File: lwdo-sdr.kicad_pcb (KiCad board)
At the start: 2 copper layers, 162 x 120 mm, 360 parts, among them J101 IN1, J102 IN2, J103 IN3, J104 IN4, J105 USB_B, J106 CLK_OUT, J107 REF_IN, J1401 Conn_02x10_Odd_Even, Q1201 NX7002AK, Q1202 PMN48XP, U1001 74LVC1G157, U1002 74LVC2G04, U1101 74LVC2GU04, U1102 74LVC2G04, U1201 TL431AFDT, U1202 TL431AFDT, U1203 TL431AFDT, U1204 MCP1824T-330, U1205 NCV8164ASN120T1G, U1206 MCP1824T-330, U1207 NCV8164ASN250T1G, U1208 NCV8164ASN330T1G, U1301 AT93C56, U1302 FT2232HL, U1401 74AVC4T245PW, U1402 74AVC4T245PW, U201 ICE40HX4K, U202 W25Q16JV, U203 IS61WV25616FBLL-10TLI, U301 THS4521ID, U401 THS4521ID, U501 THS4521ID, U601 THS4521ID, U701 AD7357xRU, U801 AD7357xRU, U901 DAC8551, U902 MCP1501-33xSN, U903 NCS325, U904 74LVC2GU04, U905 74LVC2G04, X901 DOT050V-020.0M, Y1301 12MHz CL=18p

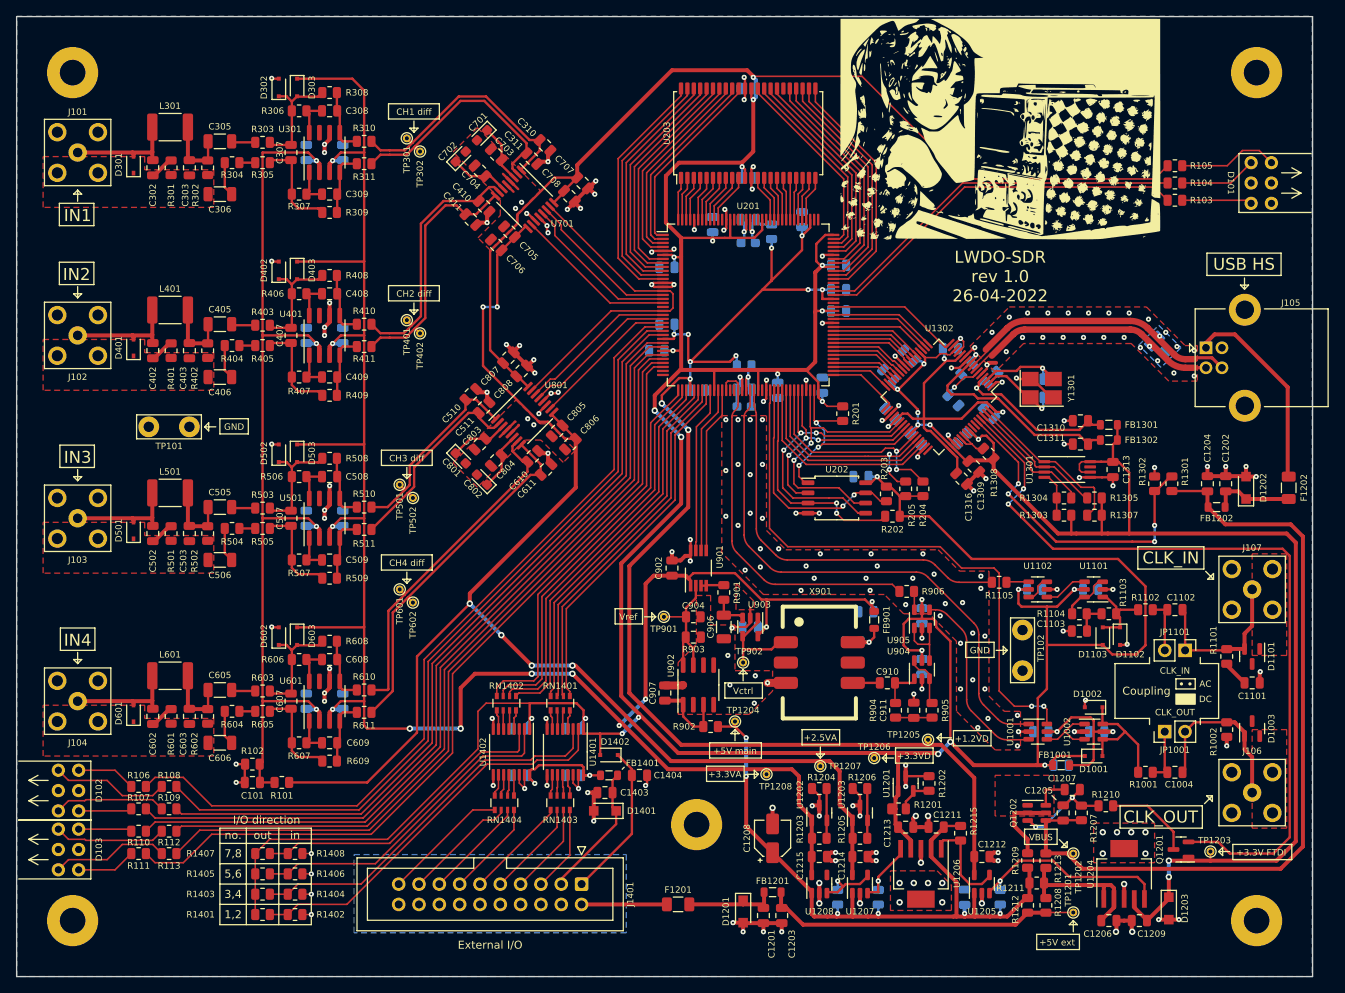
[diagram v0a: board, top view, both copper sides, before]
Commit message: Use standard Molex 73251-2201 footprint for SMA
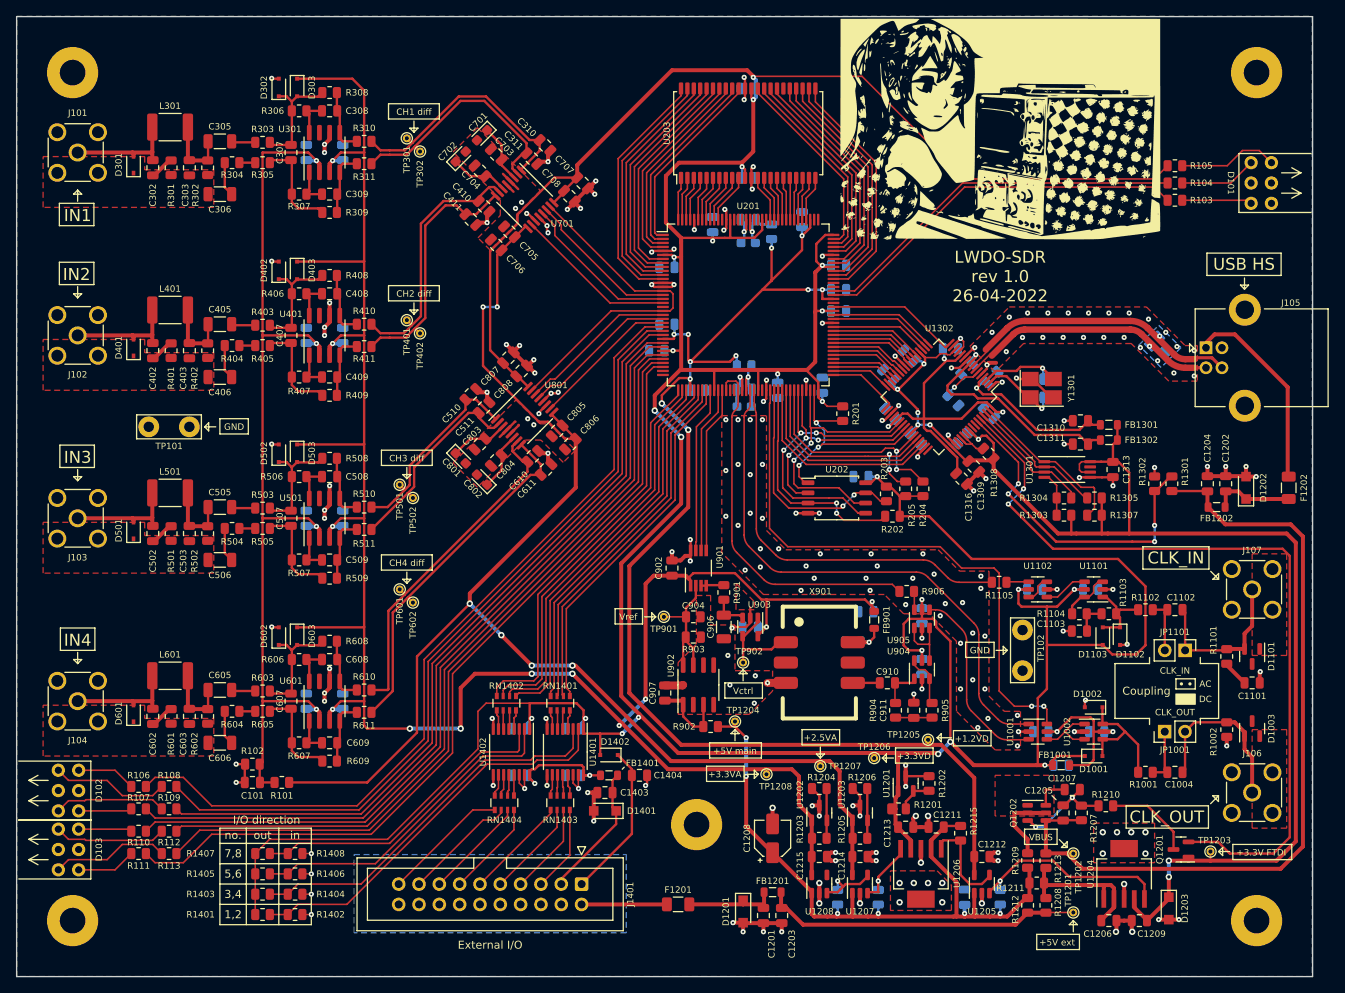
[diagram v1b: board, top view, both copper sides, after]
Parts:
- J101, J102, J103, J104, J106, J107: footprint custom-footprints:SMA_Superbat_S01-ROPT4-11BS00 -> Connector_Coaxial:SMA_Molex_73251-2200_Horizontal

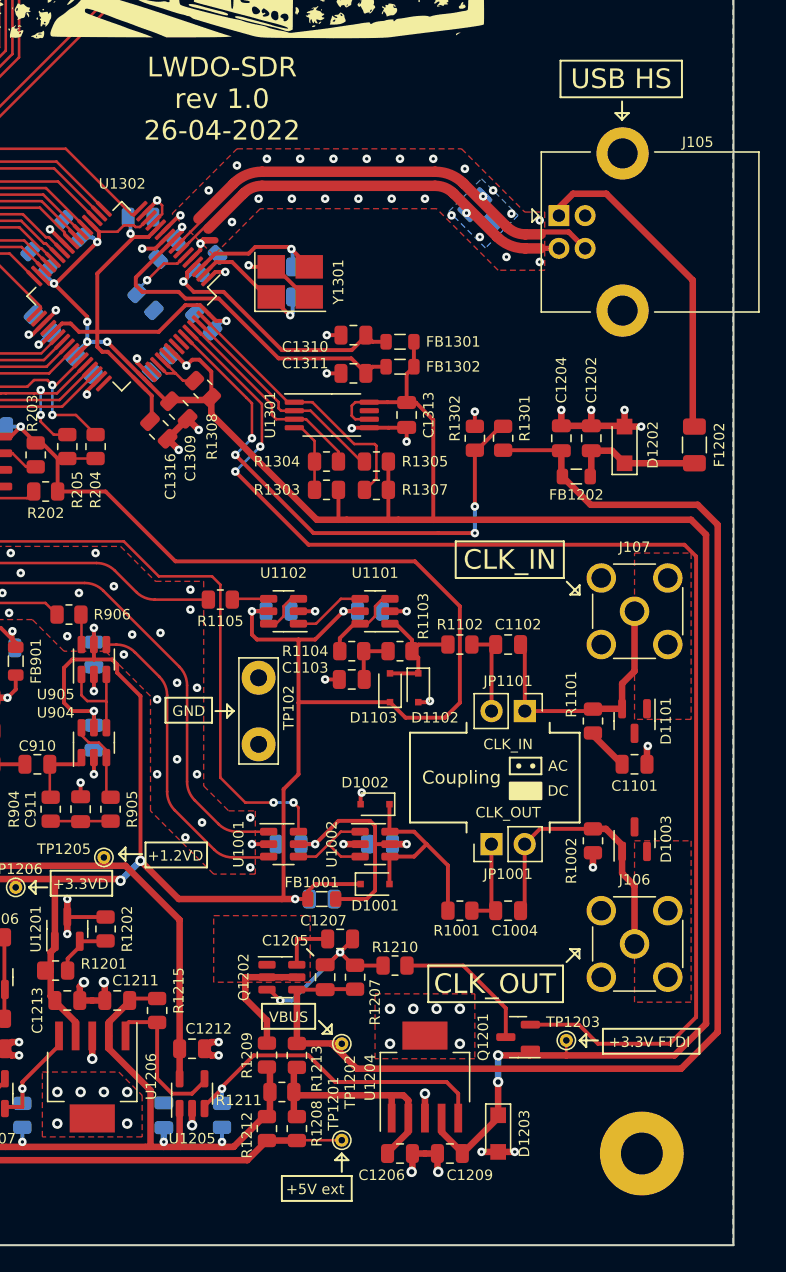
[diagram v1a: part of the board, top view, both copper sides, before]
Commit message: PCB: update attribution
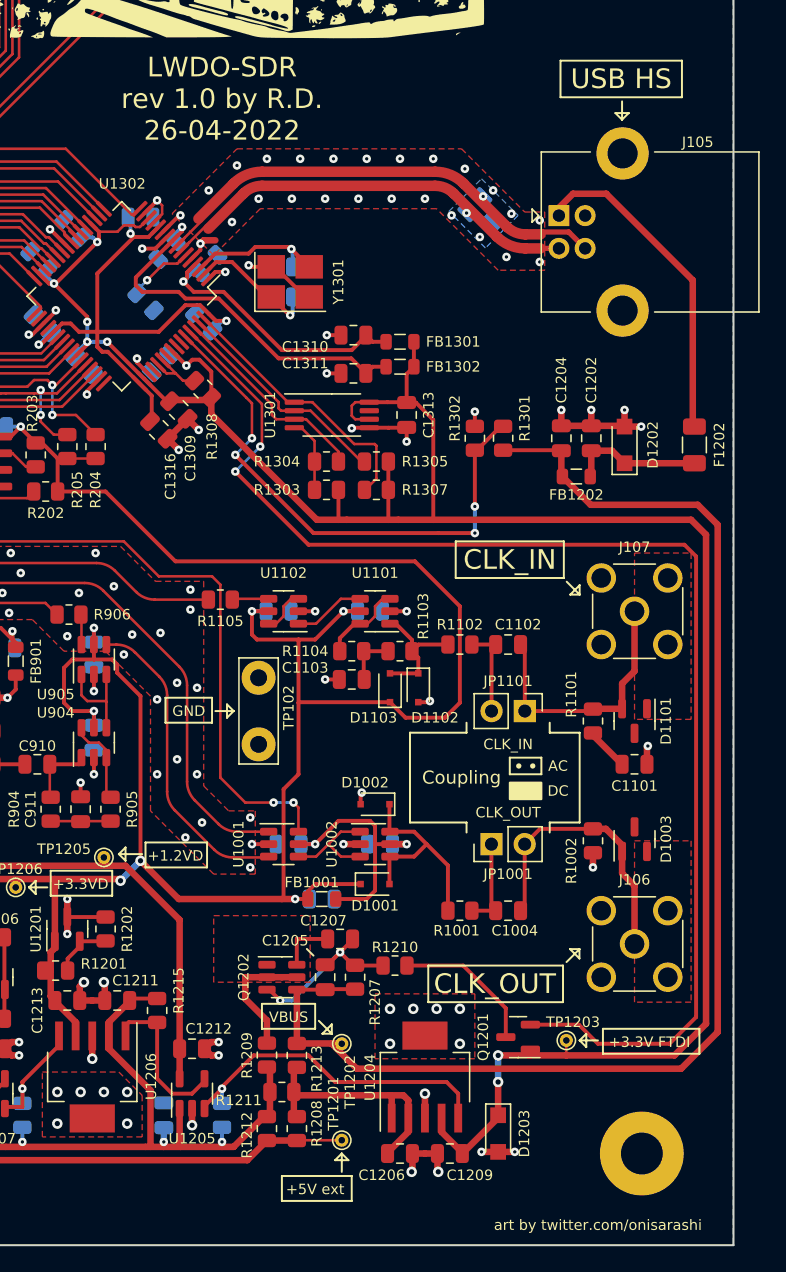
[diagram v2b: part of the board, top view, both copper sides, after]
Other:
- board text added: "LWDO-SDR rev 1.0 by R.D. 26-04-2022"
- board text added: "art by twitter.com/onisarashi"
- board text removed: "LWDO-SDR rev 1.0 26-04-2022"
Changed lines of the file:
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@@
   (gr_line (start 79 35.2) (end 249.1 35.2) (layer "Cmts.User") (width 0.15))
   (gr_rect (start 80 30) (end 242 150) (layer "Edge.Cuts") (width 0.15) (fill none))
+  (gr_text "art by twitter.com/onisarashi" (at 231.648 148.463) (layer "F.SilkS")
+    (effects (font (size 0.8 0.8) (thickness 0.127)))
+  )
   (gr_text "+3.3V FTDI" (at 235.585 134.493) (layer "F.SilkS")
     (effects (font (size 0.8 0.8) (thickness 0.127)))
@@
     (effects (font (size 1 1) (thickness 0.15)))
   )
-  (gr_text "LWDO-SDR\nrev 1.0\n26-04-2022" (at 202.946 62.484) (layer "F.SilkS")
+  (gr_text "LWDO-SDR\nrev 1.0 by R.D.\n26-04-2022" (at 202.946 62.484) (layer "F.SilkS")
     (effects (font (size 1.5 1.5) (thickness 0.15)))
   )

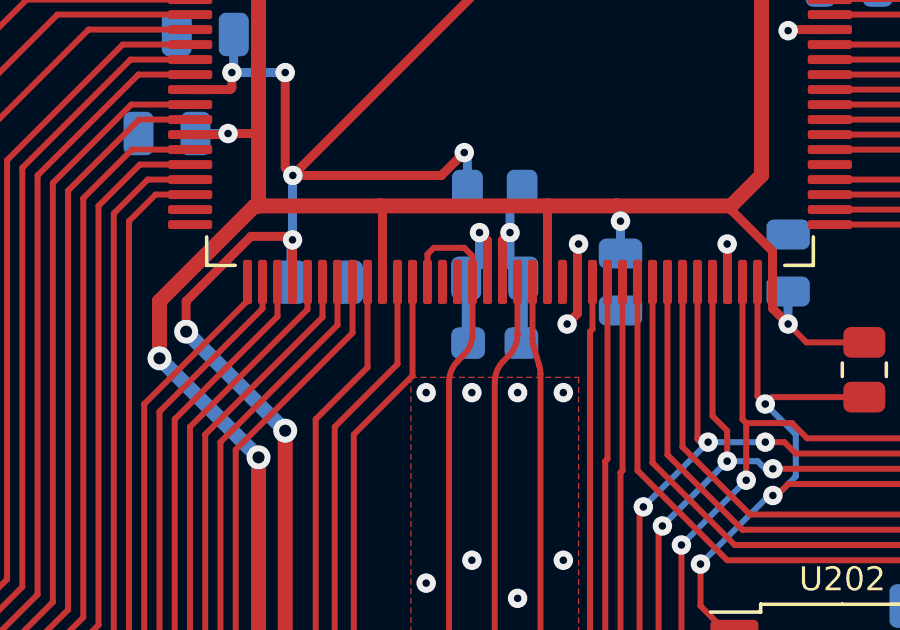
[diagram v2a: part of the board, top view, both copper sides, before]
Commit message: PCB: reroute CLK_20MHZ trace
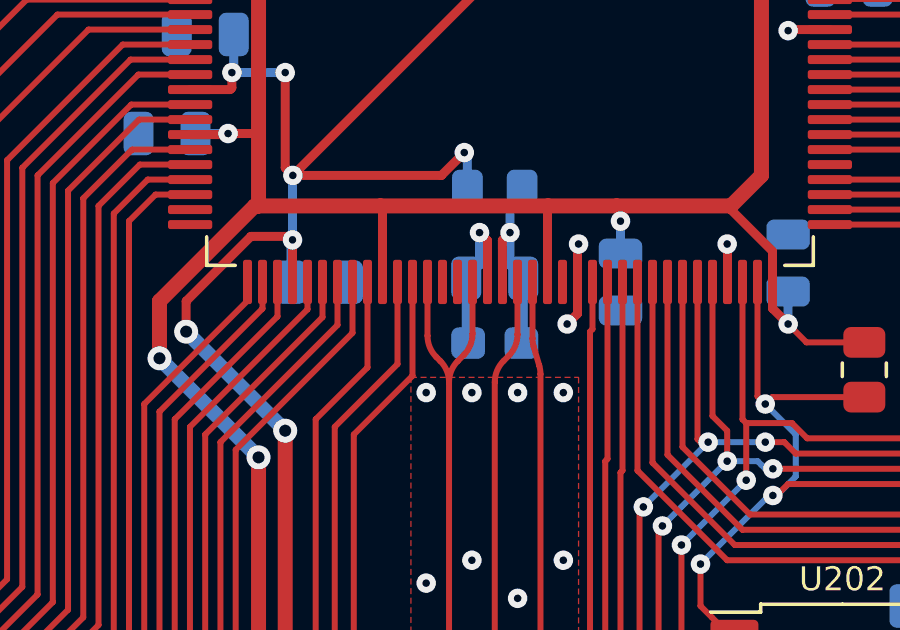
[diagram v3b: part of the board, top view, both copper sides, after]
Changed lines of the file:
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@@
   (segment (start 174.818427 100.965) (end 189.4605 100.965) (width 0.2) (layer "F.Cu") (net 183))
   (segment (start 189.4605 100.965) (end 190.3495 101.854) (width 0.2) (layer "F.Cu") (net 183))
-  (segment (start 170.2 75.839) (end 170.2 76.7025) (width 0.2) (layer "F.Cu") (net 183))
+  (segment (start 168.992893 79.203893) (end 169.125107 79.336107) (width 0.2) (layer "F.Cu") (net 183))
   (segment (start 170.2 76.7025) (end 170.2 78.432786) (width 0.2) (layer "F.Cu") (net 183))
-  (segment (start 168.7 75.775) (end 168.91 75.565) (width 0.2) (layer "F.Cu") (net 183))
-  (segment (start 168.91 75.565) (end 169.926 75.565) (width 0.2) (layer "F.Cu") (net 183))
   (segment (start 169.418 80.043214) (end 169.418 95.564573) (width 0.2) (layer "F.Cu") (net 183))
   (segment (start 169.907107 79.139893) (end 169.710893 79.336107) (width 0.2) (layer "F.Cu") (net 183))
-  (segment (start 169.926 75.565) (end 170.2 75.839) (width 0.2) (layer "F.Cu") (net 183))
-  (segment (start 168.7 76.7025) (end 168.7 75.775) (width 0.2) (layer "F.Cu") (net 183))
+  (segment (start 168.7 76.7025) (end 168.7 78.496786) (width 0.2) (layer "F.Cu") (net 183))
+  (segment (start 169.418 80.043214) (end 169.418 80.043214) (width 0.2) (layer "F.Cu") (net 183))
+  (arc (start 168.992893 79.203893) (mid 168.77612 78.87947) (end 168.7 78.496786) (width 0.2) (layer "F.Cu") (net 183))
   (arc (start 170.003787 96.978787) (mid 169.570241 96.32994) (end 169.418 95.564573) (width 0.2) (layer "F.Cu") (net 183))
+  (arc (start 169.418 80.043214) (mid 169.34188 79.660531) (end 169.125107 79.336107) (width 0.2) (layer "F.Cu") (net 183))
   (arc (start 174.818427 100.965) (mid 174.05306 100.812759) (end 173.404214 100.379214) (width 0.2) (layer "F.Cu") (net 183))
   (arc (start 170.2 78.432786) (mid 170.12388 78.815469) (end 169.907107 79.139893) (width 0.2) (layer "F.Cu") (net 183))

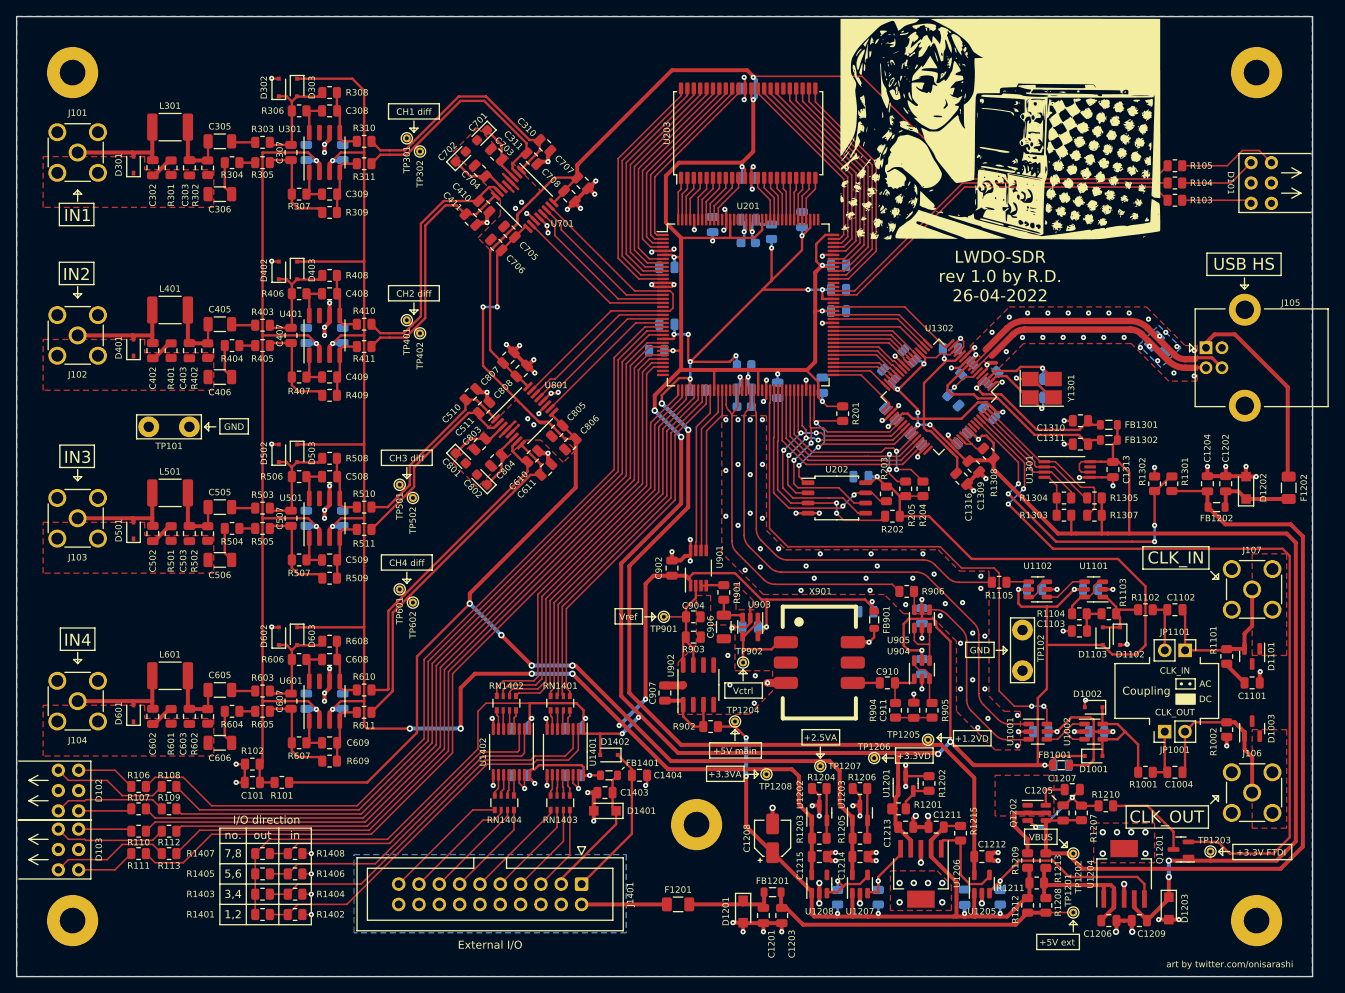
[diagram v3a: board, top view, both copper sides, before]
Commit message: PCB: improve FPGA/SRAM power routing (use zones)
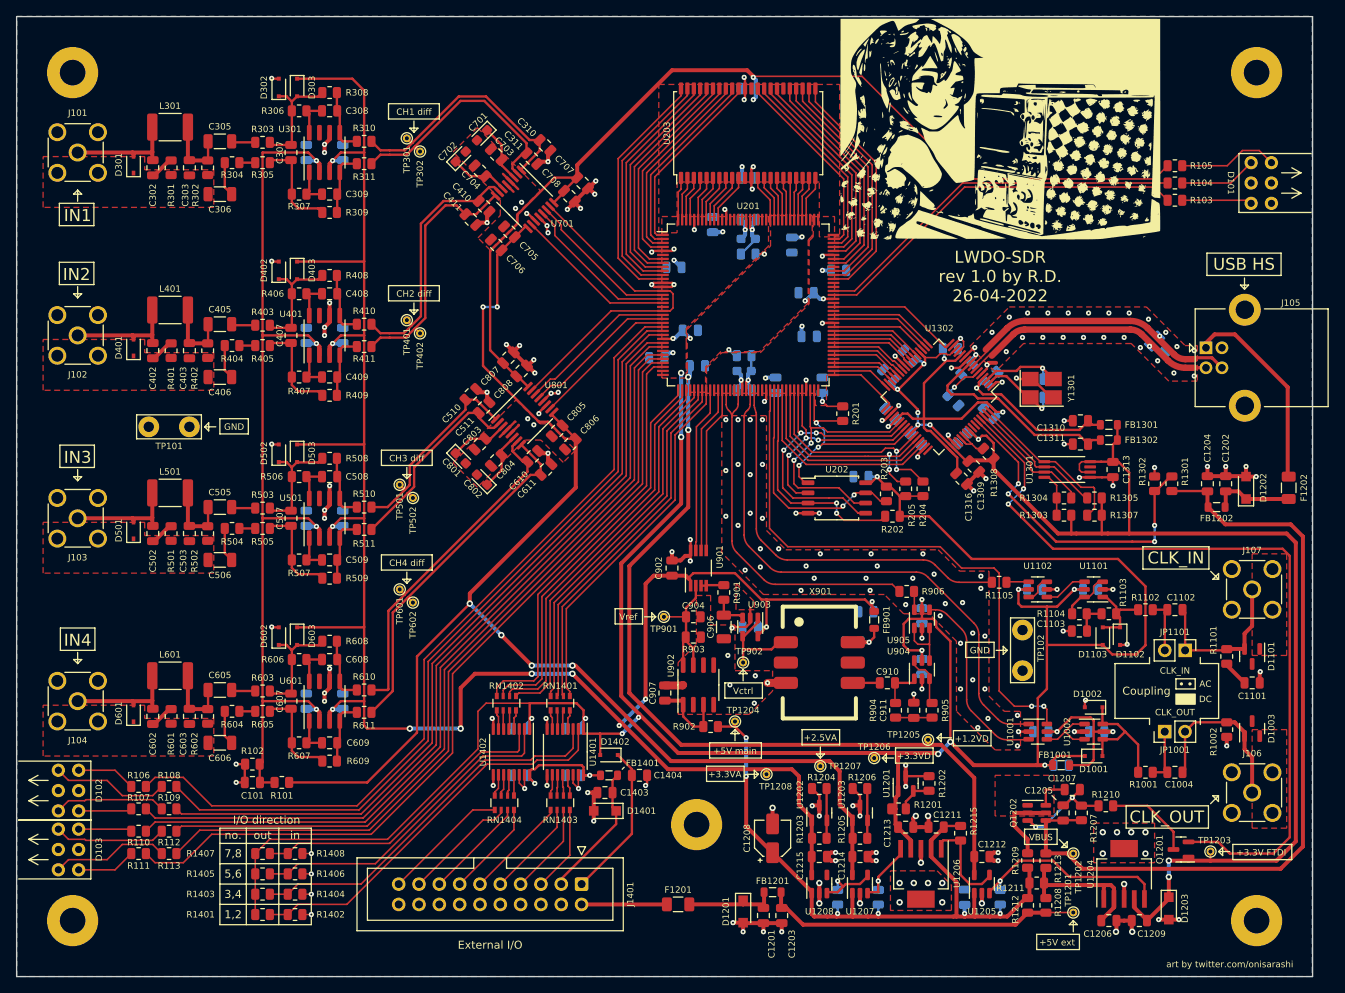
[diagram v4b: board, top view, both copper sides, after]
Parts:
- moved C208 4.86 mm to (179.1, 70.0)
- moved C217 4.44 mm to (170.9, 74.3)
- moved C207 4.08 mm to (178.7, 64.5), turned to 180 degrees
- moved R206 4.04 mm to (171.4, 59.7), turned to 0 degrees
- moved C203 3.42 mm to (176.9, 58.5), turned to -90 degrees
- moved C205 3.05 mm to (165.1, 73.7)
- moved C209 3.02 mm to (164.2, 69.2), turned to 0 degrees
- moved R207 1.27 mm to (170.9, 72.4)
- moved C204 0.89 mm to (162.2, 61.3)
- moved C214 0.89 mm to (160.0, 72.6)
- moved C212 0.68 mm to (174.9, 76.1)
- moved C201 0.63 mm to (182.8, 61.7)
- moved C215 0.51 mm to (171.4, 57.8)
- moved C218 0.13 mm to (170.9, 76.7)
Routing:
- net +3.3VD: track 595.7 -> 477.3 mm
- net +1.2VD: track 168.8 -> 116.7 mm, vias 11 -> 9
- net AGND: track 252.6 -> 249.8 mm, vias 220 -> 218
- net Net-(C217-Pad2): track 5.65 -> 4.18 mm
- net Net-(C217-Pad1): track 7.21 -> 6.04 mm
- net Net-(C215-Pad2): track 4.89 -> 4.18 mm
- added copper zone on F.Cu, net +1.2VD
- added copper zone on F.Cu, net +3.3VD
